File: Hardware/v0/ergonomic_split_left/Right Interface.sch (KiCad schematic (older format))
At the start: 0 parts

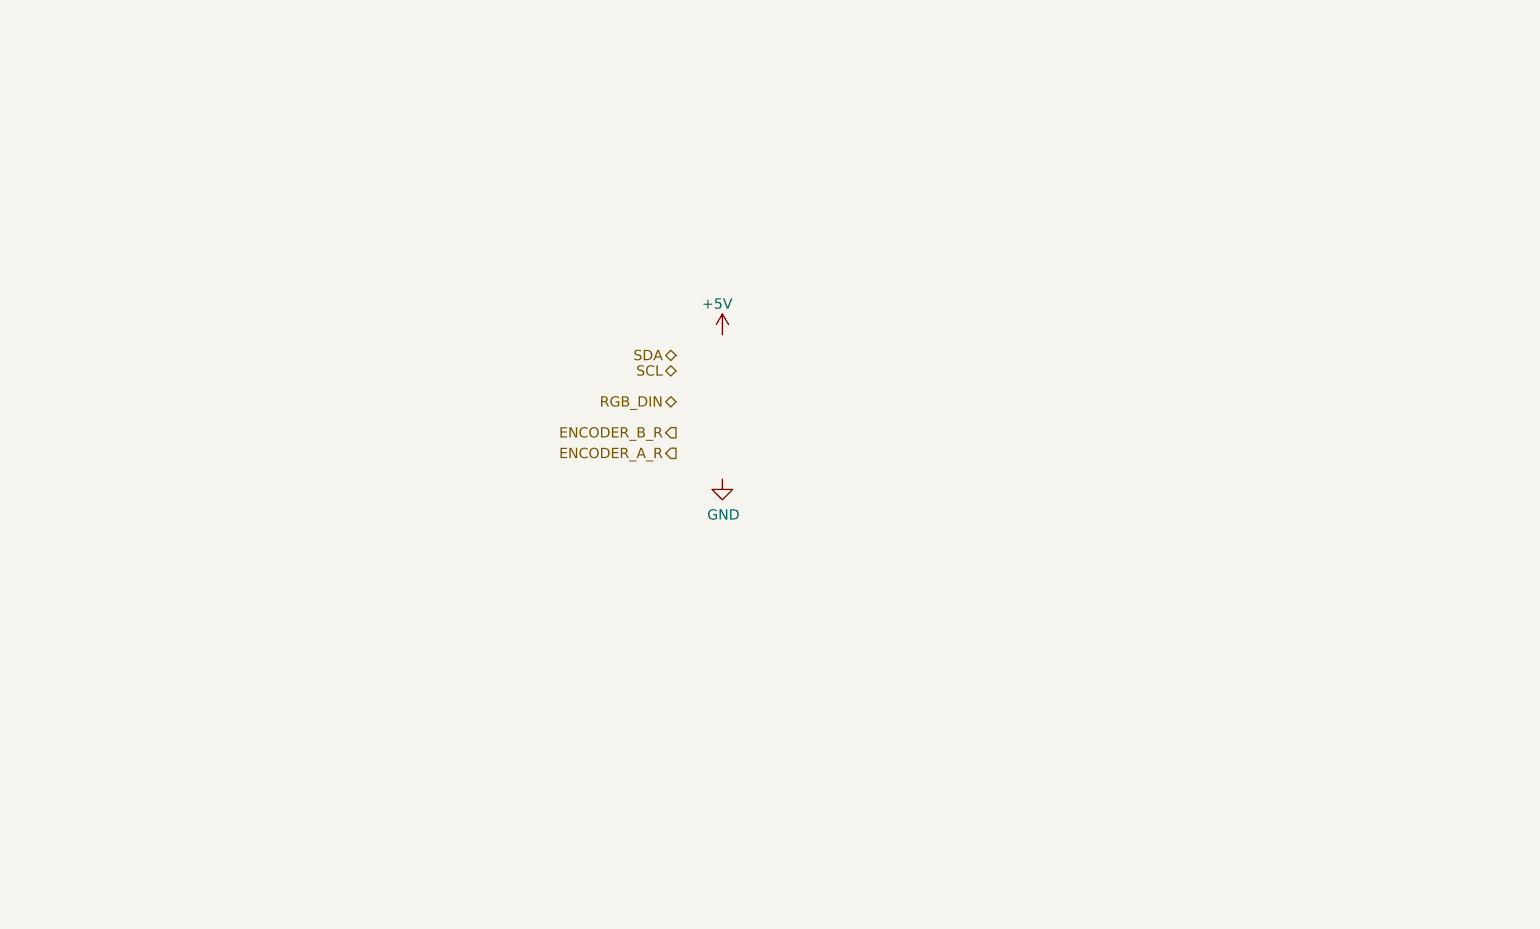
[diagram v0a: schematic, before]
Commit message: Adding power and ground planes Adding right interface USB C connector Pin swapping on ATMEGA
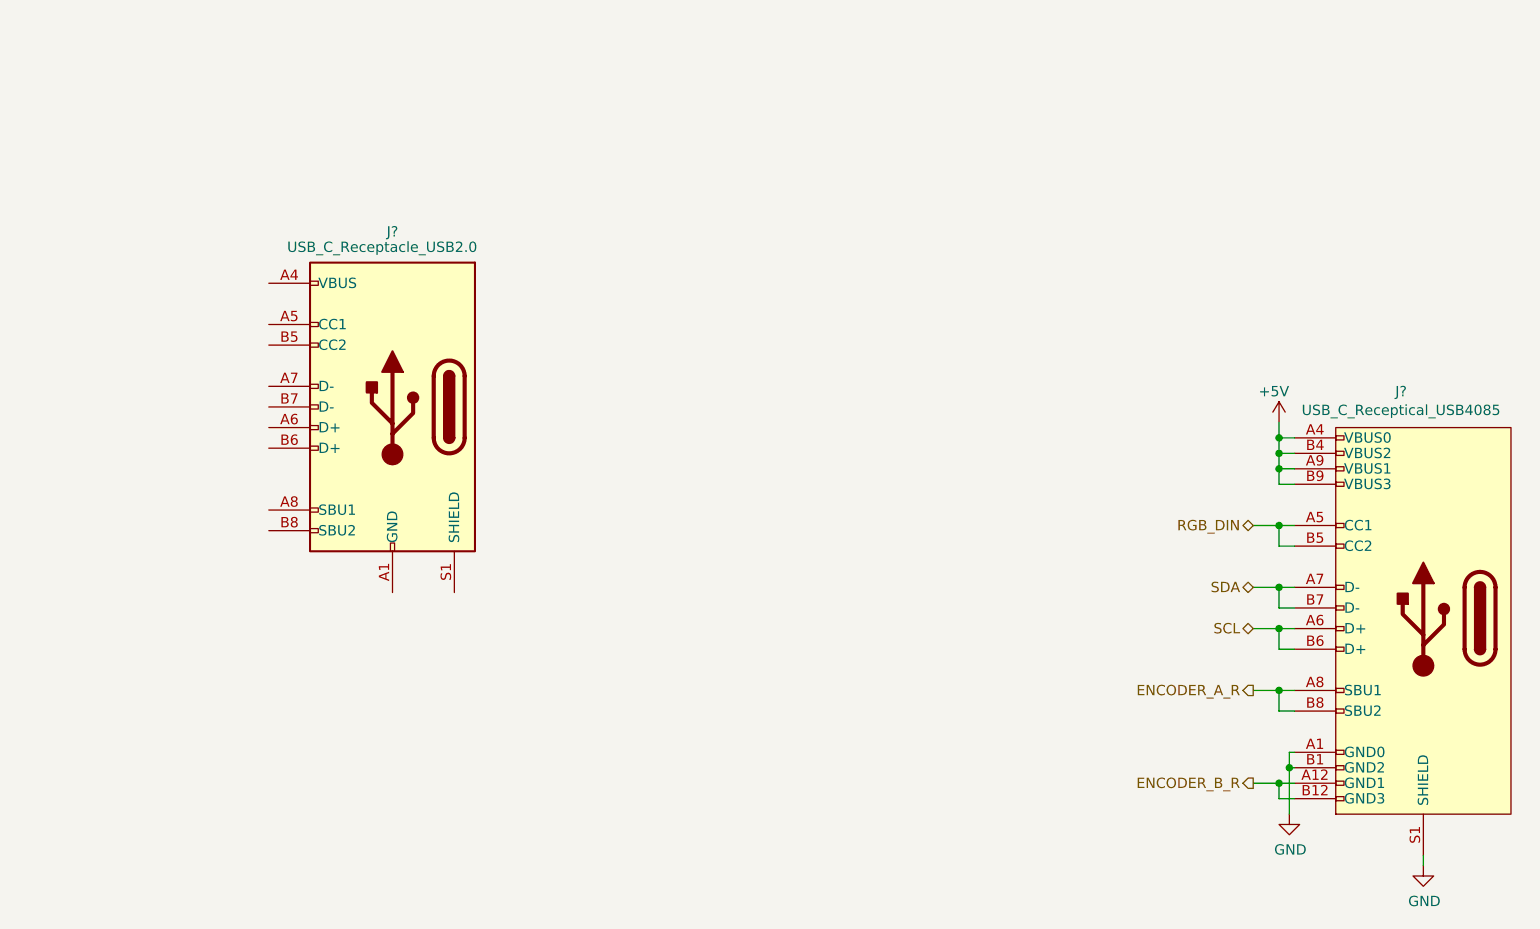
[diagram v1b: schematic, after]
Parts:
- added J?: USB_C_Receptacle_USB2.0, Connector_USB:USB_C_Receptacle_GCT_USB4085, symbol Connector:USB_C_Receptacle_USB2.0
- added J?: USB_C_Receptical_USB4085, symbol custom_parts_library:USB_C_Receptical_USB4085
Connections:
- net +5V: now also J?.A4 (VBUS0), J?.A9 (VBUS1), J?.B4 (VBUS2), J?.B9 (VBUS3)
- net ENCODER_A_R: now also J?.A8 (SBU1), J?.B8 (SBU2)
- net ENCODER_B_R: now also J?.A12 (GND1), J?.B12 (GND3)
- net GND: now also J?.A1 (GND0), J?.B1 (GND2), J?.S1 (SHIELD)
- net RGB_DIN: now also J?.A5 (CC1), J?.B5 (CC2)
- net SCL: now also J?.A6 (D+), J?.B6 (D+)
- net SDA: now also J?.A7 (D-), J?.B7 (D-)
- new net: J?.A1 (GND), J?.A12 (GND), J?.B1 (GND), J?.B12 (GND)
- new net: J?.A4 (VBUS), J?.A9 (VBUS), J?.B4 (VBUS), J?.B9 (VBUS)
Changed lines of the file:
@@
 L power:+5V #PWR?
 U 1 1 6EAD1643
-P 4175 2025
+P 6875 2450
 AR Path="/629982B4/6EAD1643" Ref="#PWR?"  Part="1"
 AR Path="/62999A71/6EAD1643" Ref="#PWR0204"  Part="1"
-F 0 "#PWR0204" H 4175 1875 50  0001 C CNN
-F 1 "+5V" H 4150 2175 50  0000 C CNN
-F 2 "" H 4175 2025 50  0001 C CNN
-F 3 "" H 4175 2025 50  0001 C CNN
-	1    4175 2025
+F 0 "#PWR0204" H 6875 2300 50  0001 C CNN
+F 1 "+5V" H 6850 2600 50  0000 C CNN
+F 2 "" H 6875 2450 50  0001 C CNN
+F 3 "" H 6875 2450 50  0001 C CNN
+	1    6875 2450
 	1    0    0    -1
 $EndComp
@@
 L power:GND #PWR?
 U 1 1 6EADCE66
-P 4175 2725
+P 6925 4350
 AR Path="/6114D32E/6EADCE66" Ref="#PWR?"  Part="1"
 AR Path="/6247A5CE/6EADCE66" Ref="#PWR?"  Part="1"
@@
 AR Path="/629982B4/6EADCE66" Ref="#PWR?"  Part="1"
 AR Path="/62999A71/6EADCE66" Ref="#PWR0206"  Part="1"
-F 0 "#PWR0206" H 4175 2475 50  0001 C CNN
-F 1 "GND" H 4180 2552 50  0000 C CNN
-F 2 "" H 4175 2725 50  0001 C CNN
-F 3 "" H 4175 2725 50  0001 C CNN
-	1    4175 2725
+F 0 "#PWR0206" H 6925 4100 50  0001 C CNN
+F 1 "GND" H 6930 4177 50  0000 C CNN
+F 2 "" H 6925 4350 50  0001 C CNN
+F 3 "" H 6925 4350 50  0001 C CNN
+	1    6925 4350
 	1    0    0    -1
 $EndComp
-Text HLabel 3950 2350 0    50   BiDi ~ 0
+Text HLabel 6750 2950 0    50   BiDi ~ 0
 RGB_DIN
-Text HLabel 3950 2125 0    50   BiDi ~ 0
+Text HLabel 6750 3250 0    50   BiDi ~ 0
 SDA
-Text HLabel 3950 2200 0    50   BiDi ~ 0
+Text HLabel 6750 3450 0    50   BiDi ~ 0
 SCL
-Text HLabel 3950 2500 0    50   Output ~ 0
+Text HLabel 6750 4200 0    50   Output ~ 0
 ENCODER_B_R
-Text HLabel 3950 2600 0    50   Output ~ 0
+Text HLabel 6750 3750 0    50   Output ~ 0
 ENCODER_A_R
+$Comp
+L Connector:USB_C_Receptacle_USB2.0 J?
+U 1 1 62D74C82
+P 2575 2375
+AR Path="/6114D32E/62D74C82" Ref="J?"  Part="1"
+AR Path="/6247A5CE/62D74C82" Ref="J?"  Part="1"
+AR Path="/612340DE/62D74C82" Ref="J?"  Part="1"
+AR Path="/62F6B81F/62D74C82" Ref="J?"  Part="1"
+AR Path="/629982B4/62D74C82" Ref="J?"  Part="1"
+AR Path="/62999A71/62D74C82" Ref="J?"  Part="1"
+F 0 "J?" H 2575 3225 50  0000 C CNN
+F 1 "USB_C_Receptacle_USB2.0" H 2625 3150 50  0000 C CNN
+F 2 "Connector_USB:USB_C_Receptacle_GCT_USB4085" H 2725 2375 50  0001 C CNN
+F 3 "https://www.usb.org/sites/default/files/documents/usb_type-c.zip" H 2725 2375 50  0001 C CNN
+	1    2575 2375
+	-1   0    0    -1
+$EndComp
+$Comp
+L custom_parts_library:USB_C_Receptical_USB4085 J?
+U 1 1 62D93B58
+P 7575 3400
+F 0 "J?" H 7683 4500 50  0000 C CNN
+F 1 "USB_C_Receptical_USB4085" H 7683 4409 50  0000 C CNN
+F 2 "" H 7600 4425 50  0001 C CNN
+F 3 "" H 7600 4425 50  0001 C CNN
+	1    7575 3400
+	-1   0    0    -1
+$EndComp
+$Comp
+L power:GND #PWR?
+U 1 1 62D970D0
+P 7575 4600
+AR Path="/6114D32E/62D970D0" Ref="#PWR?"  Part="1"
+AR Path="/6247A5CE/62D970D0" Ref="#PWR?"  Part="1"
+AR Path="/612340DE/62D970D0" Ref="#PWR?"  Part="1"
+AR Path="/62F6B81F/62D970D0" Ref="#PWR?"  Part="1"
+AR Path="/629982B4/62D970D0" Ref="#PWR?"  Part="1"
+AR Path="/62999A71/62D970D0" Ref="#PWR?"  Part="1"
+F 0 "#PWR?" H 7575 4350 50  0001 C CNN
+F 1 "GND" H 7580 4427 50  0000 C CNN
+F 2 "" H 7575 4600 50  0001 C CNN
+F 3 "" H 7575 4600 50  0001 C CNN
+	1    7575 4600
+	1    0    0    -1
+$EndComp
+Wire Wire Line
+	6875 2450 6875 2525
+Wire Wire Line
+	6875 2750 6950 2750
+Wire Wire Line
+	6950 2675 6875 2675
+Connection ~ 6875 2675
+Wire Wire Line
+	6875 2675 6875 2750
+Wire Wire Line
+	6950 2600 6875 2600
+Connection ~ 6875 2600
+Wire Wire Line
+	6875 2600 6875 2675
+Wire Wire Line
+	6950 2525 6875 2525
+Connection ~ 6875 2525
+Wire Wire Line
+	6875 2525 6875 2600
+Wire Wire Line
+	6750 2950 6875 2950
+Wire Wire Line
+	6950 3050 6875 3050
+Wire Wire Line
+	6875 3050 6875 2950
+Connection ~ 6875 2950
+Wire Wire Line
+	6875 2950 6950 2950
+Wire Wire Line
+	6750 3250 6875 3250
+Wire Wire Line
+	6950 3350 6875 3350
+Wire Wire Line
+	6875 3350 6875 3250
+Connection ~ 6875 3250
+Wire Wire Line
+	6875 3250 6950 3250
+Wire Wire Line
+	6750 3450 6875 3450
+Wire Wire Line
+	6950 3550 6875 3550
+Wire Wire Line
+	6875 3550 6875 3450
+Connection ~ 6875 3450
+Wire Wire Line
+	6875 3450 6950 3450
+Wire Wire Line
+	6750 3750 6875 3750
+Wire Wire Line
+	6950 3850 6875 3850
+Wire Wire Line
+	6875 3850 6875 3750
+Connection ~ 6875 3750
+Wire Wire Line
+	6875 3750 6950 3750
+Wire Wire Line
+	6750 4200 6875 4200
+Wire Wire Line
+	6875 4275 6875 4200
+Connection ~ 6875 4200
+Wire Wire Line
+	6875 4200 6950 4200
+Wire Wire Line
+	6875 4275 6950 4275
+Wire Wire Line
+	6925 4050 6950 4050
+Wire Wire Line
+	6950 4125 6925 4125
+Wire Wire Line
+	6925 4050 6925 4125
+Connection ~ 6925 4125
+Wire Wire Line
+	6925 4125 6925 4350
+Wire Wire Line
+	7575 4600 7575 4550
 $EndSCHEMATC

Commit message: Debug connectors Adding I2C debug header Changed SPI programming header to edge mount Changed right interface connector to IDC Cleaning up schematic
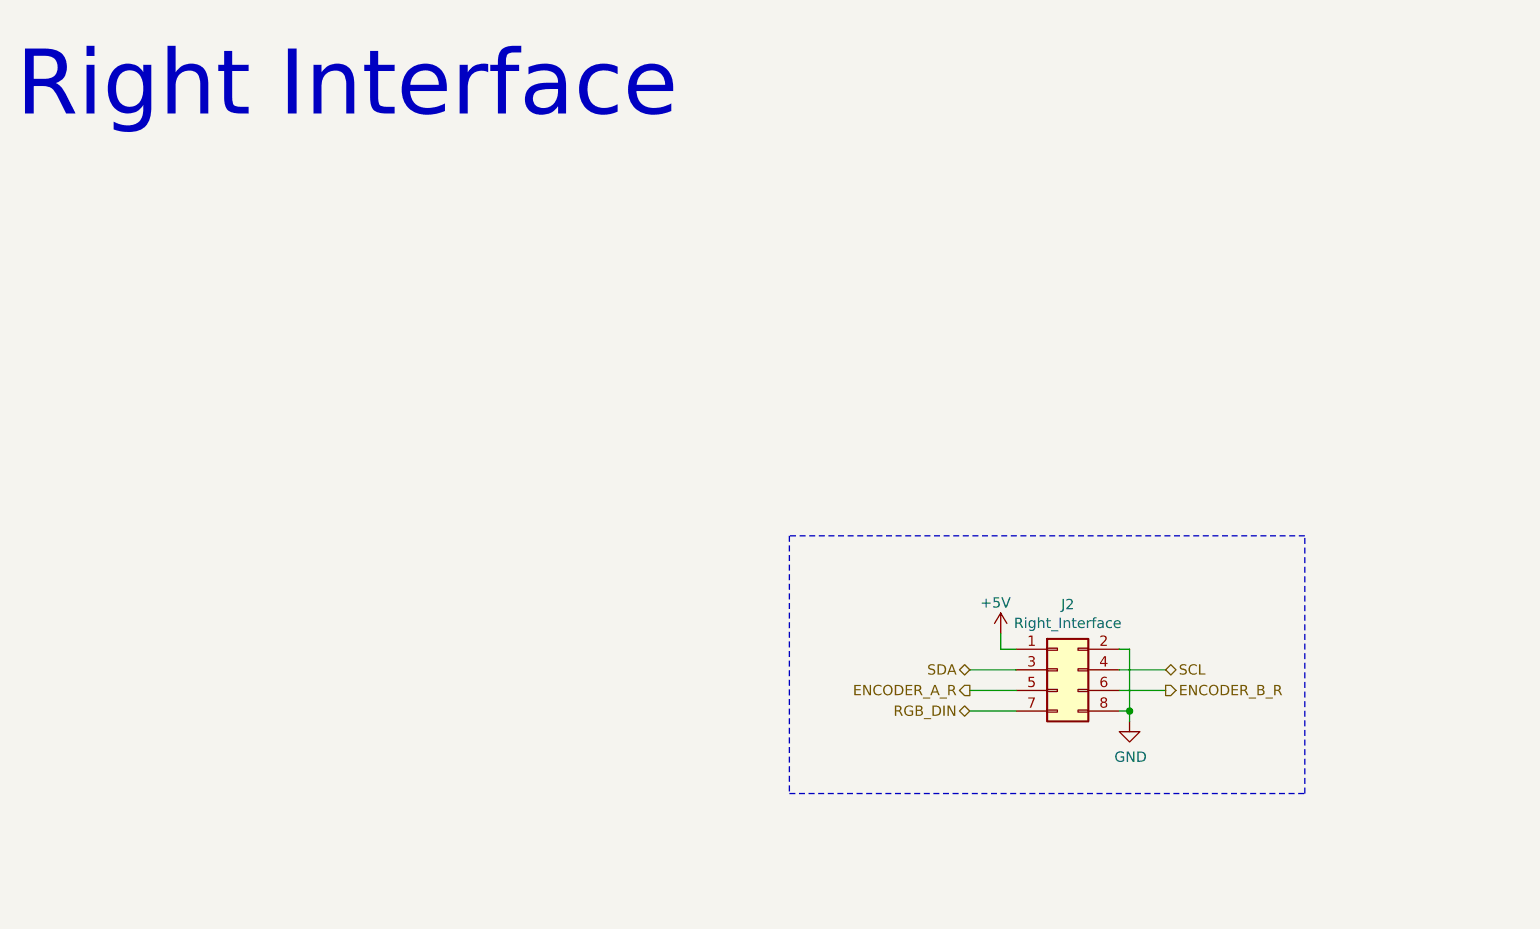
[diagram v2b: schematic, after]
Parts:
- removed J?: USB_C_Receptacle_USB2.0, Connector_USB:USB_C_Receptacle_GCT_USB4085, symbol Connector:USB_C_Receptacle_USB2.0
- removed J?: USB_C_Receptical_USB4085, symbol custom_parts_library:USB_C_Receptical_USB4085
- added J2: Right_Interface, Connector_PinHeader_2.54mm:PinHeader_2x04_P2.54mm_Horizontal, symbol Connector_Generic:Conn_02x04_Odd_Even
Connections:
- net +5V: now also J2.1 (Pin_1)
- net ENCODER_A_R: now also J2.5 (Pin_5)
- net ENCODER_B_R: now also J2.6 (Pin_6)
- net GND: now also J2.2 (Pin_2), J2.8 (Pin_8)
- net RGB_DIN: now also J2.7 (Pin_7)
- net SCL: now also J2.4 (Pin_4)
- net SDA: now also J2.3 (Pin_3)
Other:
- note added: "Right Interface"
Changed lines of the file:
@@
 L power:+5V #PWR?
 U 1 1 6EAD1643
-P 6875 2450
+P 5525 3475
 AR Path="/629982B4/6EAD1643" Ref="#PWR?"  Part="1"
 AR Path="/62999A71/6EAD1643" Ref="#PWR0204"  Part="1"
-F 0 "#PWR0204" H 6875 2300 50  0001 C CNN
-F 1 "+5V" H 6850 2600 50  0000 C CNN
-F 2 "" H 6875 2450 50  0001 C CNN
-F 3 "" H 6875 2450 50  0001 C CNN
-	1    6875 2450
+F 0 "#PWR0204" H 5525 3325 50  0001 C CNN
+F 1 "+5V" H 5500 3625 50  0000 C CNN
+F 2 "" H 5525 3475 50  0001 C CNN
+F 3 "" H 5525 3475 50  0001 C CNN
+	1    5525 3475
 	1    0    0    -1
 $EndComp
-$Comp
-L power:GND #PWR?
-U 1 1 6EADCE66
-P 6925 4350
-AR Path="/6114D32E/6EADCE66" Ref="#PWR?"  Part="1"
-AR Path="/6247A5CE/6EADCE66" Ref="#PWR?"  Part="1"
-AR Path="/612340DE/6EADCE66" Ref="#PWR?"  Part="1"
-AR Path="/62F6B81F/6EADCE66" Ref="#PWR?"  Part="1"
-AR Path="/629982B4/6EADCE66" Ref="#PWR?"  Part="1"
-AR Path="/62999A71/6EADCE66" Ref="#PWR0206"  Part="1"
-F 0 "#PWR0206" H 6925 4100 50  0001 C CNN
-F 1 "GND" H 6930 4177 50  0000 C CNN
-F 2 "" H 6925 4350 50  0001 C CNN
-F 3 "" H 6925 4350 50  0001 C CNN
-	1    6925 4350
-	1    0    0    -1
-$EndComp
-Text HLabel 6750 2950 0    50   BiDi ~ 0
-RGB_DIN
-Text HLabel 6750 3250 0    50   BiDi ~ 0
-SDA
-Text HLabel 6750 3450 0    50   BiDi ~ 0
-SCL
-Text HLabel 6750 4200 0    50   Output ~ 0
+Text HLabel 6325 3750 2    50   Output ~ 0
 ENCODER_B_R
-Text HLabel 6750 3750 0    50   Output ~ 0
+Text HLabel 5375 3750 0    50   Output ~ 0
 ENCODER_A_R
-$Comp
-L Connector:USB_C_Receptacle_USB2.0 J?
-U 1 1 62D74C82
-P 2575 2375
-AR Path="/6114D32E/62D74C82" Ref="J?"  Part="1"
-AR Path="/6247A5CE/62D74C82" Ref="J?"  Part="1"
-AR Path="/612340DE/62D74C82" Ref="J?"  Part="1"
-AR Path="/62F6B81F/62D74C82" Ref="J?"  Part="1"
-AR Path="/629982B4/62D74C82" Ref="J?"  Part="1"
-AR Path="/62999A71/62D74C82" Ref="J?"  Part="1"
-F 0 "J?" H 2575 3225 50  0000 C CNN
-F 1 "USB_C_Receptacle_USB2.0" H 2625 3150 50  0000 C CNN
-F 2 "Connector_USB:USB_C_Receptacle_GCT_USB4085" H 2725 2375 50  0001 C CNN
-F 3 "https://www.usb.org/sites/default/files/documents/usb_type-c.zip" H 2725 2375 50  0001 C CNN
-	1    2575 2375
-	-1   0    0    -1
-$EndComp
-$Comp
-L custom_parts_library:USB_C_Receptical_USB4085 J?
-U 1 1 62D93B58
-P 7575 3400
-F 0 "J?" H 7683 4500 50  0000 C CNN
-F 1 "USB_C_Receptical_USB4085" H 7683 4409 50  0000 C CNN
-F 2 "" H 7600 4425 50  0001 C CNN
-F 3 "" H 7600 4425 50  0001 C CNN
-	1    7575 3400
-	-1   0    0    -1
-$EndComp
 $Comp
 L power:GND #PWR?
 U 1 1 62D970D0
-P 7575 4600
+P 6150 3900
 AR Path="/6114D32E/62D970D0" Ref="#PWR?"  Part="1"
 AR Path="/6247A5CE/62D970D0" Ref="#PWR?"  Part="1"
@@
 AR Path="/62F6B81F/62D970D0" Ref="#PWR?"  Part="1"
 AR Path="/629982B4/62D970D0" Ref="#PWR?"  Part="1"
-AR Path="/62999A71/62D970D0" Ref="#PWR?"  Part="1"
-F 0 "#PWR?" H 7575 4350 50  0001 C CNN
-F 1 "GND" H 7580 4427 50  0000 C CNN
-F 2 "" H 7575 4600 50  0001 C CNN
-F 3 "" H 7575 4600 50  0001 C CNN
-	1    7575 4600
+AR Path="/62999A71/62D970D0" Ref="#PWR018"  Part="1"
+F 0 "#PWR018" H 6150 3650 50  0001 C CNN
+F 1 "GND" H 6155 3727 50  0000 C CNN
+F 2 "" H 6150 3900 50  0001 C CNN
+F 3 "" H 6150 3900 50  0001 C CNN
+	1    6150 3900
 	1    0    0    -1
 $EndComp
+$Comp
+L Connector_Generic:Conn_02x04_Odd_Even J2
+U 1 1 62DC873B
+P 5800 3650
+F 0 "J2" H 5850 3967 50  0000 C CNN
+F 1 "Right_Interface" H 5850 3876 50  0000 C CNN
+F 2 "Connector_PinHeader_2.54mm:PinHeader_2x04_P2.54mm_Horizontal" H 5800 3650 50  0001 C CNN
+F 3 "~" H 5800 3650 50  0001 C CNN
+	1    5800 3650
+	1    0    0    -1
+$EndComp
+Text HLabel 5375 3850 0    50   BiDi ~ 0
+RGB_DIN
+Text HLabel 6325 3650 2    50   BiDi ~ 0
+SCL
+Text HLabel 5375 3650 0    50   BiDi ~ 0
+SDA
 Wire Wire Line
-	6875 2450 6875 2525
+	5525 3475 5525 3550
 Wire Wire Line
-	6875 2750 6950 2750
+	5525 3550 5600 3550
 Wire Wire Line
-	6950 2675 6875 2675
-Connection ~ 6875 2675
+	5375 3650 5600 3650
 Wire Wire Line
-	6875 2675 6875 2750
+	5375 3750 5600 3750
 Wire Wire Line
-	6950 2600 6875 2600
-Connection ~ 6875 2600
+	5600 3850 5375 3850
 Wire Wire Line
-	6875 2600 6875 2675
+	6100 3650 6325 3650
 Wire Wire Line
-	6950 2525 6875 2525
-Connection ~ 6875 2525
+	6100 3750 6325 3750
 Wire Wire Line
-	6875 2525 6875 2600
+	6150 3900 6150 3850
 Wire Wire Line
-	6750 2950 6875 2950
+	6150 3550 6100 3550
 Wire Wire Line
-	6950 3050 6875 3050
+	6100 3850 6150 3850
+Connection ~ 6150 3850
 Wire Wire Line
-	6875 3050 6875 2950
-Connection ~ 6875 2950
-Wire Wire Line
-	6875 2950 6950 2950
-Wire Wire Line
-	6750 3250 6875 3250
-Wire Wire Line
-	6950 3350 6875 3350
-Wire Wire Line
-	6875 3350 6875 3250
-Connection ~ 6875 3250
-Wire Wire Line
-	6875 3250 6950 3250
-Wire Wire Line
-	6750 3450 6875 3450
-Wire Wire Line
-	6950 3550 6875 3550
-Wire Wire Line
-	6875 3550 6875 3450
-Connection ~ 6875 3450
-Wire Wire Line
-	6875 3450 6950 3450
-Wire Wire Line
-	6750 3750 6875 3750
-Wire Wire Line
-	6950 3850 6875 3850
-Wire Wire Line
-	6875 3850 6875 3750
-Connection ~ 6875 3750
-Wire Wire Line
-	6875 3750 6950 3750
-Wire Wire Line
-	6750 4200 6875 4200
-Wire Wire Line
-	6875 4275 6875 4200
-Connection ~ 6875 4200
-Wire Wire Line
-	6875 4200 6950 4200
-Wire Wire Line
-	6875 4275 6950 4275
-Wire Wire Line
-	6925 4050 6950 4050
-Wire Wire Line
-	6950 4125 6925 4125
-Wire Wire Line
-	6925 4050 6925 4125
-Connection ~ 6925 4125
-Wire Wire Line
-	6925 4125 6925 4350
-Wire Wire Line
-	7575 4600 7575 4550
+	6150 3850 6150 3550
+Text Notes 750  1000 0    315  ~ 0
+Right Interface
+Wire Notes Line
+	4500 4250 7000 4250
+Wire Notes Line
+	4500 3000 4500 4250
+Wire Notes Line
+	7000 4250 7000 3000
+Wire Notes Line
+	7000 3000 4500 3000
 $EndSCHEMATC
